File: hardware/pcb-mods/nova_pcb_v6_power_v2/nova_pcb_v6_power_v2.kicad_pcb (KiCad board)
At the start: 4 copper layers, 112 x 90 mm, 61 parts, among them J1 XT60_4S_IN, J12 XT30_JET_12V, J13 XT30_L2_12V, J14 XT30_Arm7V5, J2 UBEC_5V_AUX, J20 IB_2x06, J3 XT30_Inj, J4 XT30_Inj, J5 XT30_Inj, J6 XT30_Inj, J7 XT30_Inj, J8 ServoBus_TTL, M1 Voltmeter_DC, Q1 IRLB3034PBF, Q2 BSS138_cutoff, Q3 BSS138_estop, Q4 BSS138_jetcut, SW1 Contura_SPST_18A, SW2 Estop_NC_latching, U1 Pololu_D42V110F7_LEG_7V5, U10 INA226, U11 INA226, U12 INA226, U2 Pololu_D42V110F12_HIP_12V, U3 Pololu_D24V22F12_L2_12V, U4 Pololu_D42V55F12_JET_12V, U5 Pololu_D42V55F7_ARM_7V5, U8 LM393, U9 INA226

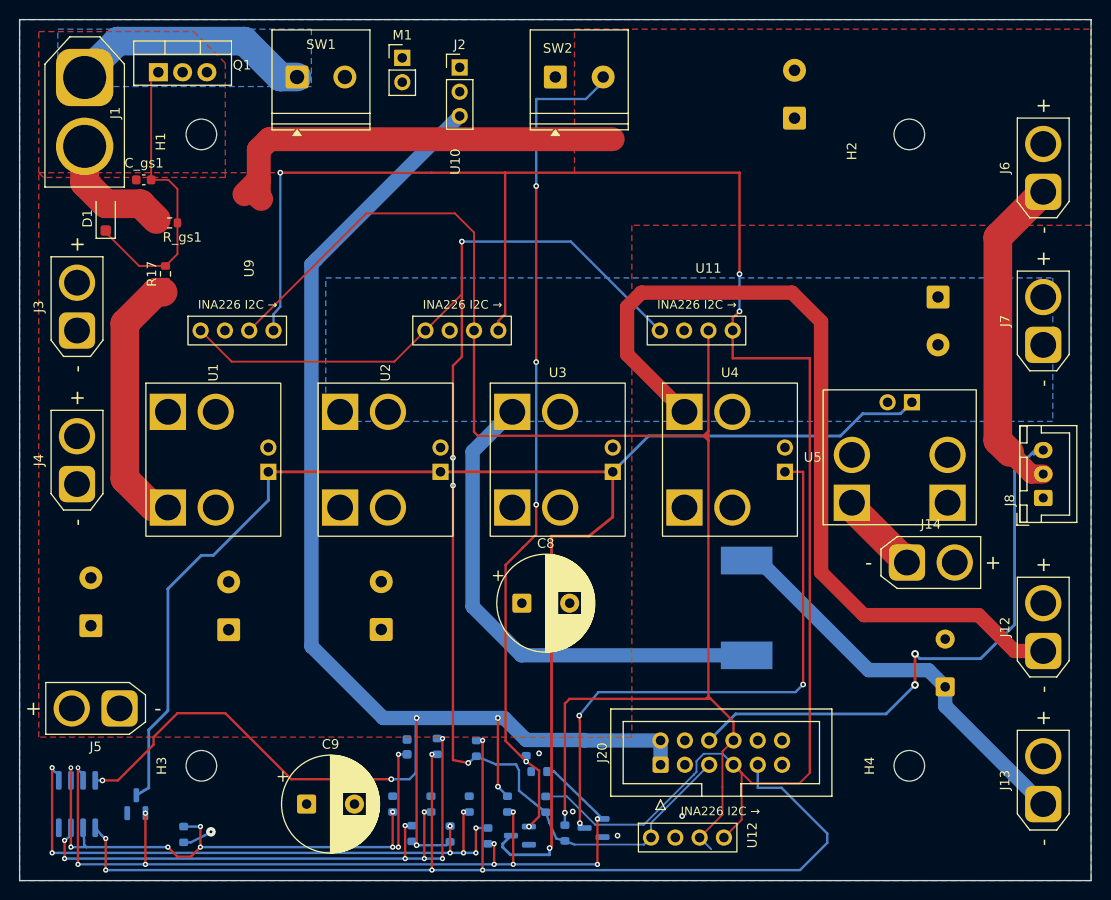
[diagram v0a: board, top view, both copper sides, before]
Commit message: power board: fix reversed XT connector polarity (all 9 AMASS XT)
AMASS XT footprints number pad1=chamfer/NEGATIVE, pad2=flat/POSITIVE.
Board had +V wired to pad1 -> every keyed power connector reverse-wired:
J1 (XT60 battery in), J3-J7 (rail injection), J12-J14 (Jetson/L2/arm out).
Mating a normally-built cable would feed +V to the - terminal and fry the
connected load (Jetson, servos, arm). Confirmed against footprint flat/chamfer
geometry + physical connector (flat=+).

Fix: swapped pin1/pin2 net assignment on all 9 connectors in schematic,
re-routed PCB, regenerated 14-file gerber set. Pololu bucks use a custom
non-keyed terminal (pad1=rect=+V) and were correctly left unchanged.

Verify: ERC 0, DRC 0 hard / 0 unconnected, fab_gate GO, J20 match intact.

Co-Authored-By: Claude Opus 4.8 <noreply@anthropic.com>
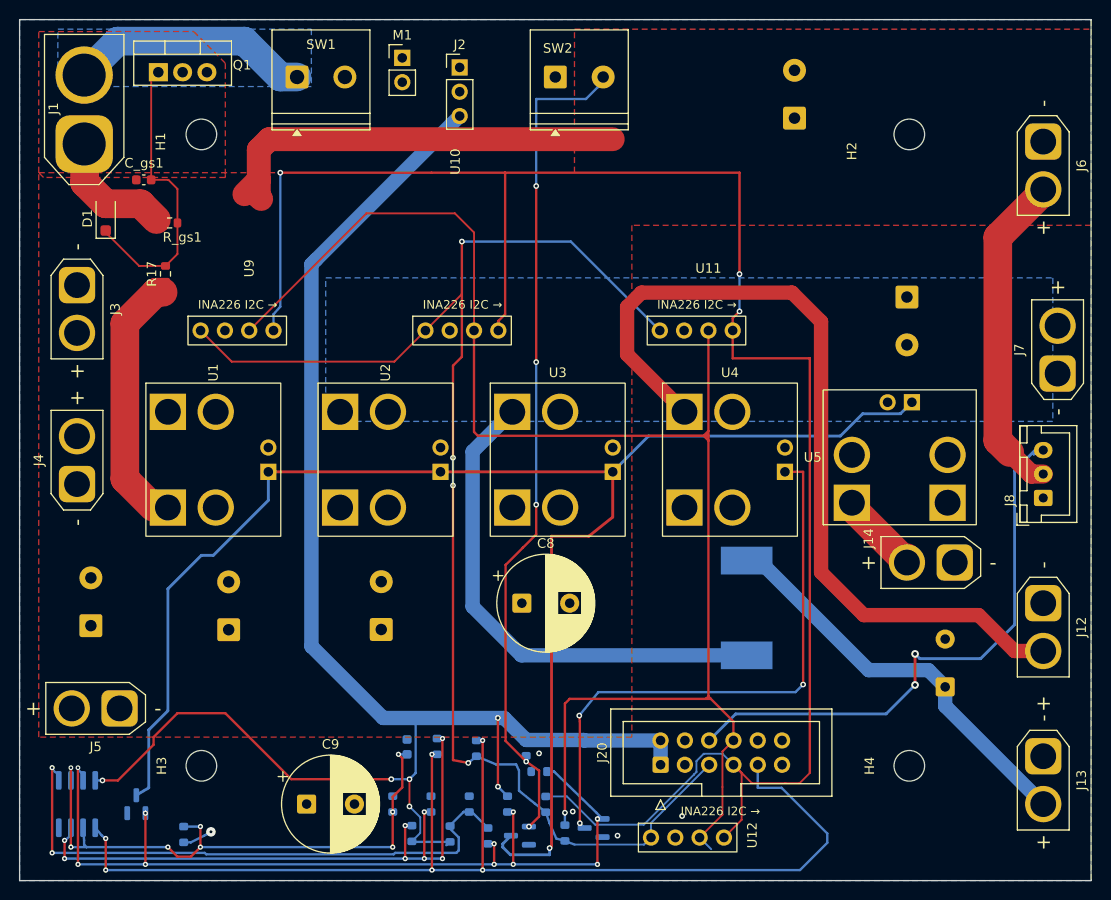
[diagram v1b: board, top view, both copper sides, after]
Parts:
- SW1: value Contura_SPST_18A -> Rocker_30A
- moved J1 6.95 mm to (90.8, 64.0), turned to 90 degrees
- moved J6 5.25 mm to (191.0, 63.8), turned to -90 degrees
- moved J12 5.00 mm to (191.0, 112.0), turned to -90 degrees
- moved J13 5.00 mm to (191.0, 128.0), turned to -90 degrees
- moved J14 5.00 mm to (181.8, 107.8), turned to 180 degrees
- moved J3 4.75 mm to (90.0, 78.8), turned to -90 degrees
- moved J7 3.35 mm to (192.5, 88.0)
- moved C5 3.25 mm to (176.8, 80.0)
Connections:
- J1 pad 1: /01 Battery Input + Reverse Protection/VBAT -> /01 Battery Input + Reverse Protection/BATT_NEG
- J1 pad 2: /01 Battery Input + Reverse Protection/BATT_NEG -> /01 Battery Input + Reverse Protection/VBAT
- J12 pad 1: V12_JET -> GND
- J12 pad 2: GND -> V12_JET
- J13 pad 1: V12_L2 -> GND
- J13 pad 2: GND -> V12_L2
- J14 pad 1: V7V5_ARM -> GND
- J14 pad 2: GND -> V7V5_ARM
- J3 pad 1: V7V5_LEG -> GND
- J3 pad 2: GND -> V7V5_LEG
- J4 pad 1: V7V5_LEG -> GND
- J4 pad 2: GND -> V7V5_LEG
- J5 pad 1: V7V5_LEG -> GND
- J5 pad 2: GND -> V7V5_LEG
- J6 pad 1: V7V5_LEG -> GND
- J6 pad 2: GND -> V7V5_LEG
- J7 pad 1: V12_HIP -> GND
- J7 pad 2: GND -> V12_HIP
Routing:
- net V5_AUX: track 176.9 -> 171.2 mm
- net /06 Safety Chain/VREF_H: track 66.4 -> 62.1 mm, vias 8 -> 2
- net /06 Safety Chain/VSENSE: track 65.0 -> 61.3 mm, vias 9 -> 8
- net /06 Safety Chain/VREF_G: track 65.9 -> 66.6 mm

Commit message: power board: solid 3mm V12_HIP trace to J7 pad2 (kill hip thermal throat)
J7 (hip-rail injection) +V pad connected to the V12_HIP pour by thermal relief
only (1.5mm spokes) — DRC-legal but a current-density throat at worst-case
all-4-hips-stall (~11A). Added a 3.0mm B.Cu trace from the hip bulk cap to
J7 pad2 → ~14A+ @ 2oz solid path, throat eliminated. Belt-and-suspenders;
the other connectors were already adequate.

DRC 0/0, fab_gate GO, polarity intact, gerbers regenerated.

Co-Authored-By: Claude Opus 4.8 <noreply@anthropic.com>
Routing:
- net V12_HIP: track 0.00 -> 17.0 mm

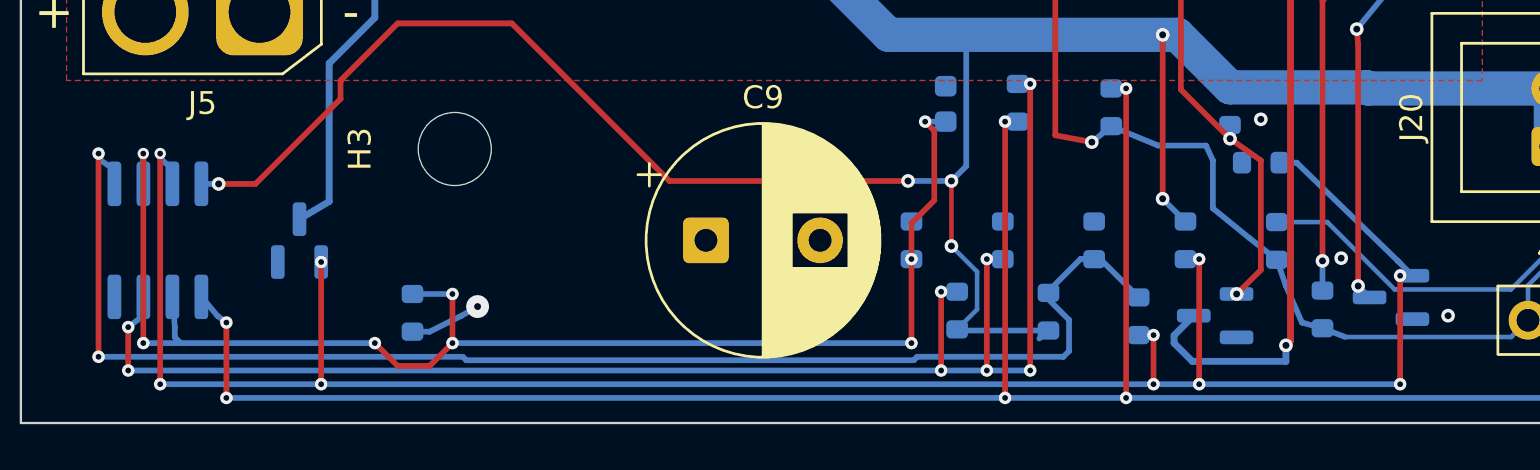
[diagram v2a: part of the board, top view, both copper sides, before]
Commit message: power board: via-annular cleanup in safety cluster (zero sub-nominal)
Relieved the dense VSENSE/HARDCUT cluster: moved HARDCUT via off VSENSE
(edge gap 0.24->0.68mm), grew both to full 0.15mm annular. Every via now
>=0.15mm annular (0 sub-nominal, was 2). No net/polarity change; DRC 0/0,
fab_gate GO. Gerbers regenerated.

Co-Authored-By: Claude Opus 4.8 <noreply@anthropic.com>
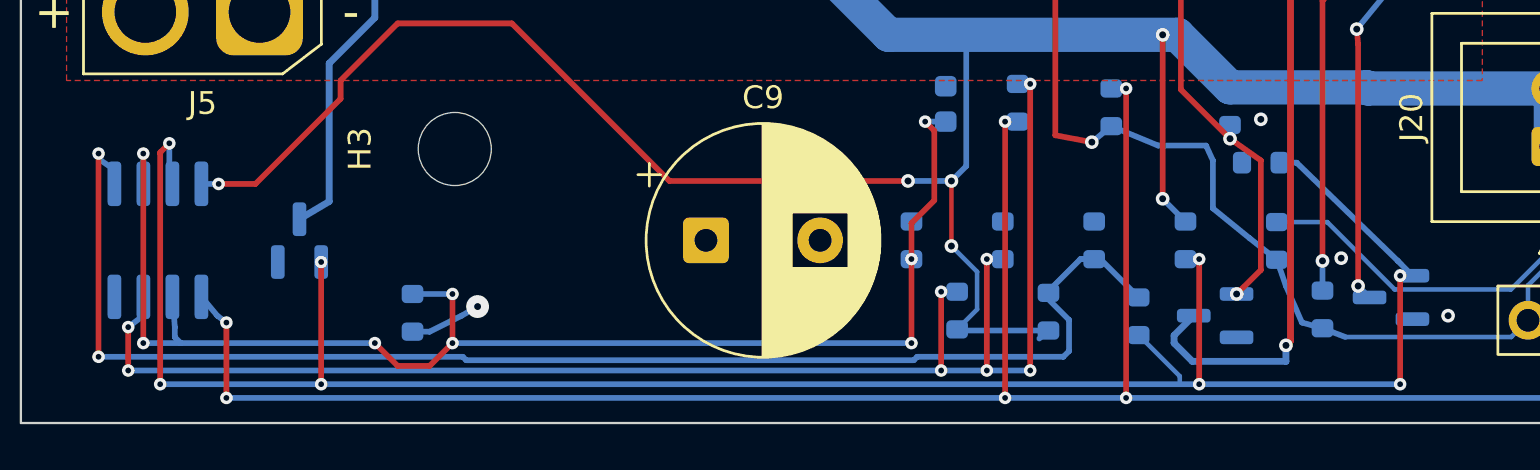
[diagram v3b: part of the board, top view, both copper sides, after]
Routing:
- net /06 Safety Chain/HARDCUT: track 93.3 -> 94.9 mm, vias 10 -> 8
